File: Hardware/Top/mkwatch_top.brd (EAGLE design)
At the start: 38 x 38 mm, 64 parts, among them SW5 SWITCH.MOM, SW6 SWITCH.MOM, U1 NRF52832_MODULE_MDBT42, U4 FT231XS, U5 PCF8523

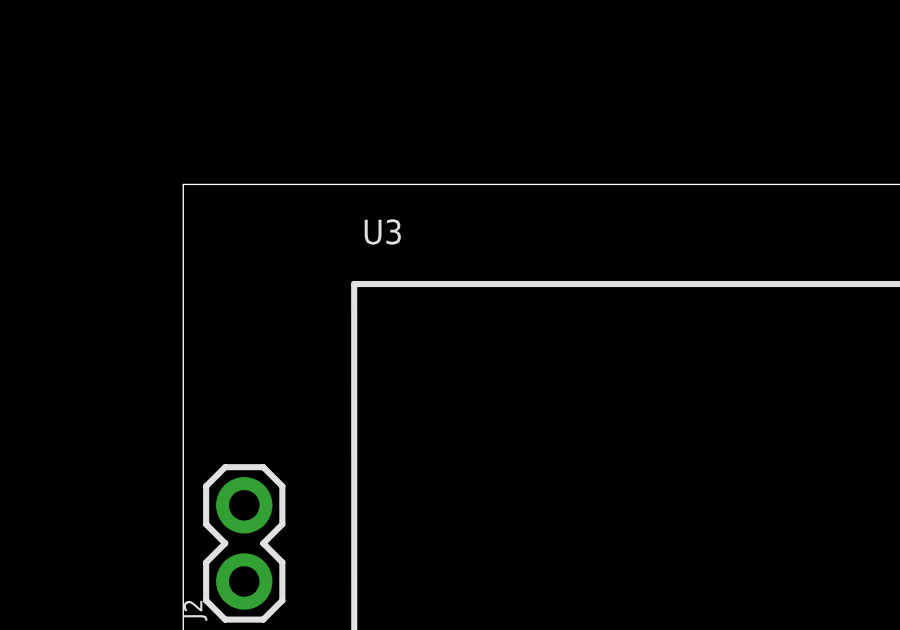
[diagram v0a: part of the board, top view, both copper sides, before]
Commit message: added 7pin connector to schematic and board for comm between top and bottom board
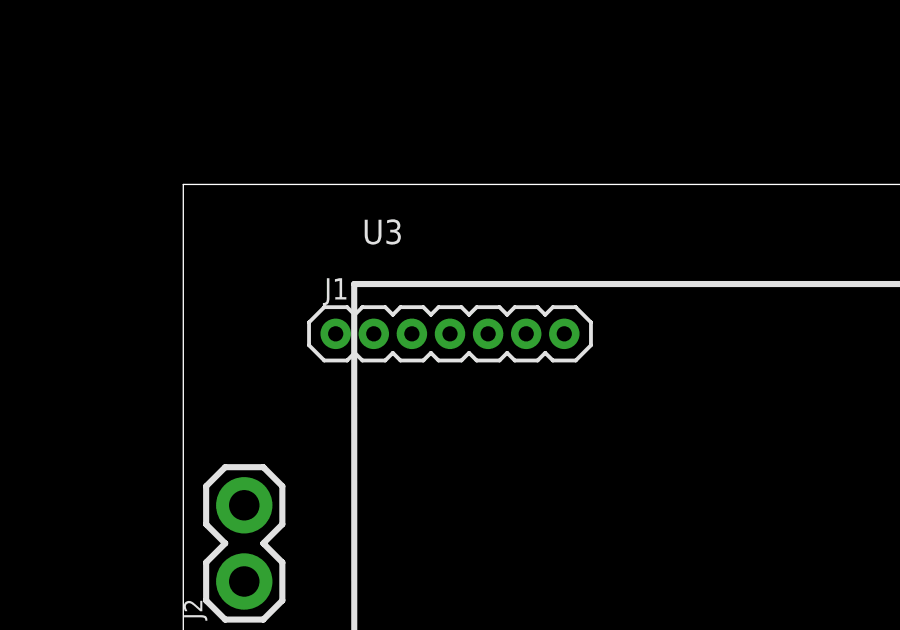
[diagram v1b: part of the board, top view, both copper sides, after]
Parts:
- added J1: (no value), LinnesLab-Connectors:1X07_1.27MM
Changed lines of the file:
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@@
 <attribute name="VALUE" x="-66.675" y="-17.145" size="1.27" layer="27"/>
+</element>
+<element name="J1" library="LinnesLab-Connectors" package="1X07_1.27MM" value="" x="5.08" y="33.02" smashed="yes">
+<attribute name="NAME" x="4.699" y="34.163" size="0.7112" layer="25"/>
+<attribute name="VALUE" x="4.572" y="31.115" size="0.7112" layer="27" ratio="20"/>
 </element>
 </elements>

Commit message: WIP - positioned main components on top and bottom, starting to re arrange passives before routing begins
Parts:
- moved LED2 109.4 mm to (34.2, 19.3), turned to 270 degrees
- moved LED1 107.6 mm to (35.9, 19.3), turned to 270 degrees
- moved R2 103.0 mm to (34.2, 22.6), turned to 90 degrees
- moved R1 101.2 mm to (35.9, 22.6), turned to 90 degrees
- moved U4 91.7 mm to (5.21, 7.04)
- moved L1 78.9 mm to (17.9, 28.4)
- moved CORTEX2 77.4 mm to (35.7, 29.2), turned to 90 degrees
- moved C5 76.9 mm to (13.8, 24.8), turned to 180 degrees
- moved SW1 74.4 mm to (34.9, 35.7)
- moved C4 74.1 mm to (13.8, 23.2), turned to 180 degrees
- moved XTAL1 69.2 mm to (18.3, 24.1), turned to 90 degrees
- moved C6 65.6 mm to (17.8, 31.8)
- moved U5 65.5 mm to (26.7, 11.4), turned to 180 degrees
- moved C1 64.6 mm to (17.9, 30.0)
- moved C2 57.3 mm to (13.8, 21.7)
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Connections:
- new net N$16: J1.7
- new net N$18: J1.6
- new net N$19: J1.5
- new net N$27: J1.3
- new net N$28: J1.2
- new net N$29: J1.1
- net 3.3V: now also R9.2
- net N$20: now also J1.4; no longer R9.2
